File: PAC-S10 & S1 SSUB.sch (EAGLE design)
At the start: 177 parts, among them IC1 TLV1117, IC10 LM324D, IC14 TC51832F-10, IC15 315-5476A, IC21 TC51832F-10, IC33 LC7881M, IC34 NJM844GD, IC35 MC33079D, IC37 LM4558D, IC38 LM4558D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

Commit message: Add files via upload
Q14 is diode connected, uploading corrected files
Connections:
- removed net N$23: IC43.OUT, Q14.C, R65.2, R66.1
- net MRES: now also IC43.OUT, Q14.C, R65.2, R66.1

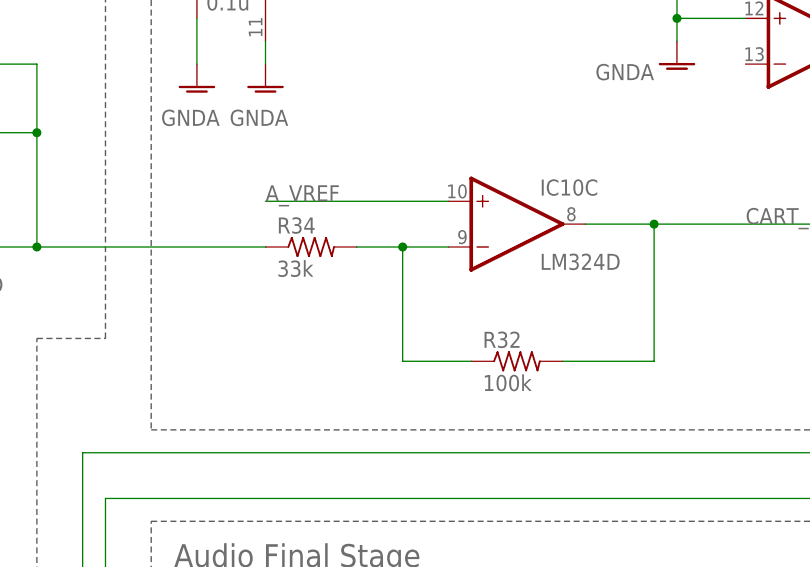
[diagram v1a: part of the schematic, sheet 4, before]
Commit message: Add files via upload
Corrected resistor reference designators (R32, R34)
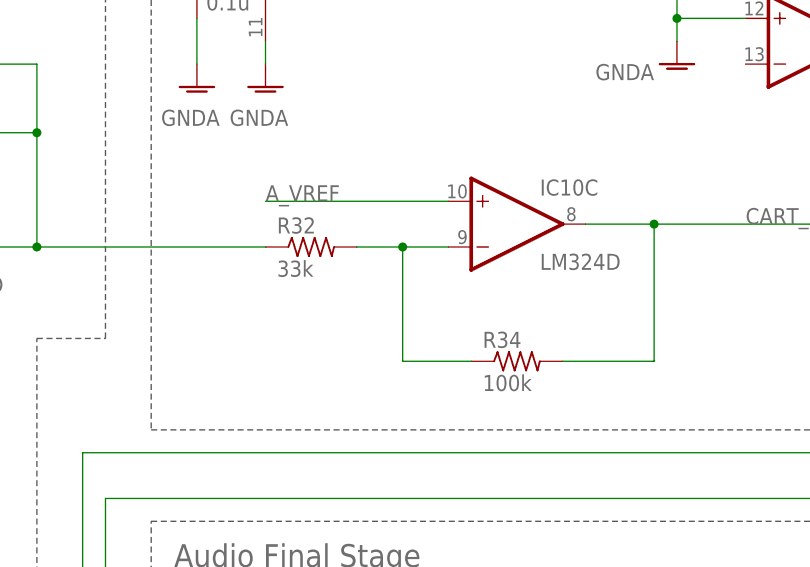
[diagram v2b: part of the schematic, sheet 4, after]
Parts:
- R32: value 100k -> 33k
- R34: value 33k -> 100k
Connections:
- net CART_R+: now also R34.2; no longer R32.2
- net N$46: now also R32.2, R34.1; no longer R32.1, R34.2
- net N$49: now also R32.1; no longer R34.1
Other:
- moved on the sheet: R32, R34
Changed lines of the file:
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@@
 <part name="GND12" library="supply1" library_urn="urn:adsk.eagle:library:371" deviceset="GNDA" device=""/>
 <part name="GND13" library="supply1" library_urn="urn:adsk.eagle:library:371" deviceset="GNDA" device=""/>
-<part name="R34" library="rcl" library_urn="urn:adsk.eagle:library:334" deviceset="R-US_" device="R0805" package3d_urn="urn:adsk.eagle:package:23553/2" value="33k"/>
-<part name="R32" library="rcl" library_urn="urn:adsk.eagle:library:334" deviceset="R-US_" device="R0805" package3d_urn="urn:adsk.eagle:package:23553/2" value="100k"/>
+<part name="R32" library="rcl" library_urn="urn:adsk.eagle:library:334" deviceset="R-US_" device="R0805" package3d_urn="urn:adsk.eagle:package:23553/2" value="33k"/>
+<part name="R34" library="rcl" library_urn="urn:adsk.eagle:library:334" deviceset="R-US_" device="R0805" package3d_urn="urn:adsk.eagle:package:23553/2" value="100k"/>
 <part name="R31" library="rcl" library_urn="urn:adsk.eagle:library:334" deviceset="R-US_" device="R0805" package3d_urn="urn:adsk.eagle:package:23553/2" value="33k"/>
 <part name="R33" library="rcl" library_urn="urn:adsk.eagle:library:334" deviceset="R-US_" device="R0805" package3d_urn="urn:adsk.eagle:package:23553/2" value="100k"/>
@@
 <attribute name="VALUE" x="299.72" y="193.04" size="1.778" layer="96" rot="R180"/>
 </instance>
-<instance part="R34" gate="G$1" x="261.62" y="172.72" smashed="yes">
+<instance part="R32" gate="G$1" x="261.62" y="172.72" smashed="yes">
 <attribute name="NAME" x="257.81" y="174.2186" size="1.778" layer="95"/>
 <attribute name="VALUE" x="257.81" y="169.418" size="1.778" layer="96"/>
 </instance>
-<instance part="R32" gate="G$1" x="284.48" y="160.02" smashed="yes">
+<instance part="R34" gate="G$1" x="284.48" y="160.02" smashed="yes">
 <attribute name="NAME" x="280.67" y="161.5186" size="1.778" layer="95"/>
 <attribute name="VALUE" x="280.67" y="156.718" size="1.778" layer="96"/>
@@
 <wire x1="231.14" y1="172.72" x2="256.54" y2="172.72" width="0.1524" layer="91"/>
 <junction x="231.14" y="172.72"/>
-<pinref part="R34" gate="G$1" pin="1"/>
+<pinref part="R32" gate="G$1" pin="1"/>
 </segment>
 </net>
@@
 <segment>
 <pinref part="IC10" gate="C" pin="-IN"/>
-<pinref part="R34" gate="G$1" pin="2"/>
+<pinref part="R32" gate="G$1" pin="2"/>
 <wire x1="276.86" y1="172.72" x2="271.78" y2="172.72" width="0.1524" layer="91"/>
-<pinref part="R32" gate="G$1" pin="1"/>
+<pinref part="R34" gate="G$1" pin="1"/>
 <wire x1="271.78" y1="172.72" x2="266.7" y2="172.72" width="0.1524" layer="91"/>
 <wire x1="279.4" y1="160.02" x2="271.78" y2="160.02" width="0.1524" layer="91"/>
@@
 <net name="CART_R+" class="0">
 <segment>
-<pinref part="R32" gate="G$1" pin="2"/>
+<pinref part="R34" gate="G$1" pin="2"/>
 <wire x1="289.56" y1="160.02" x2="299.72" y2="160.02" width="0.1524" layer="91"/>
 <wire x1="299.72" y1="160.02" x2="299.72" y2="175.26" width="0.1524" layer="91"/>
